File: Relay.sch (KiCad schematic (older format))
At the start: 11 parts

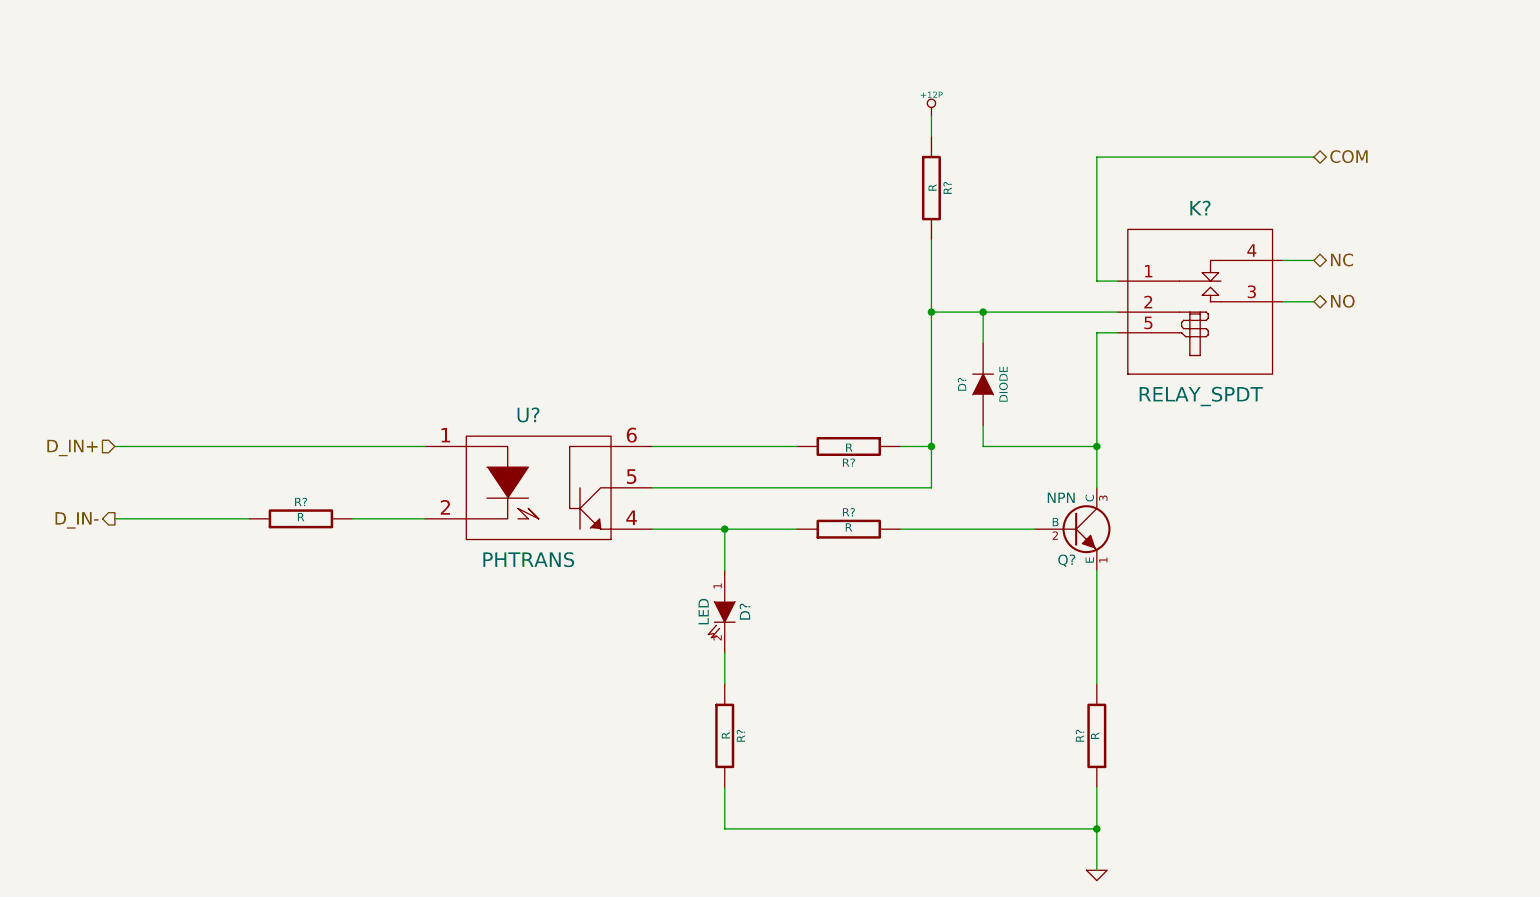
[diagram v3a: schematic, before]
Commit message: Completed Arduino Block Diagram and Fan Redesign
The commits as of this are now up to date with the videos released for
Contextual Electronics, Week 3.
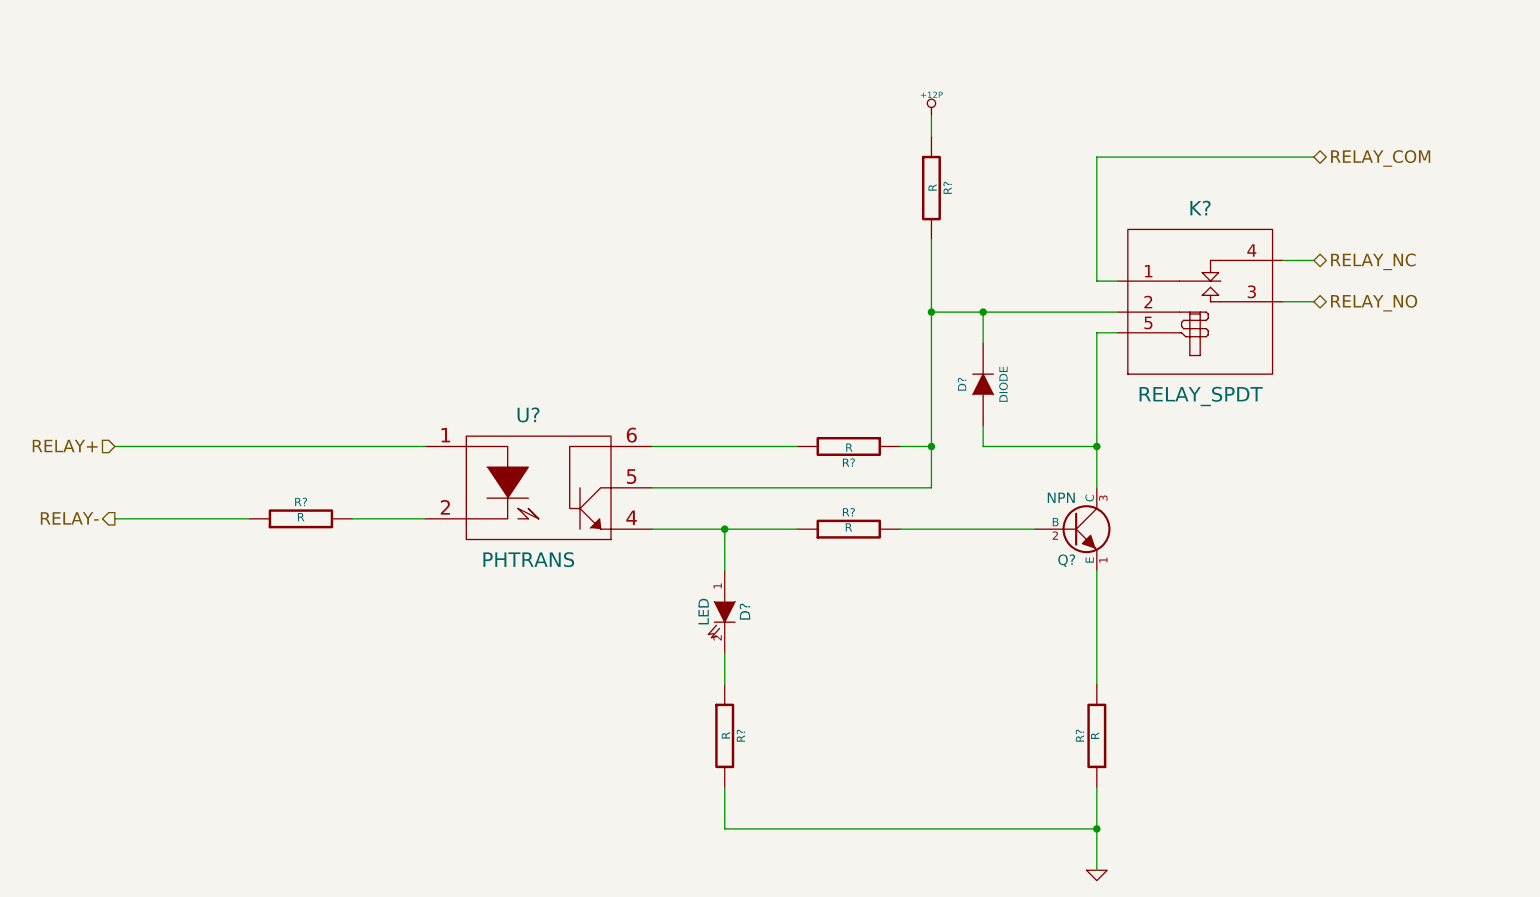
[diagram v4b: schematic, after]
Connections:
- net COM renamed RELAY_COM
- net D_IN+ renamed RELAY+
- net D_IN- renamed RELAY-
- net NC renamed RELAY_NC
- net NO renamed RELAY_NO
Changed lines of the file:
@@
 $Descr A4 11693 8268
 encoding utf-8
-Sheet 4 9
+Sheet 3 9
 Title ""
 Date "6 feb 2014"
@@
 $EndDescr
 Text HLabel 2350 3700 0    60   Input ~ 0
-D_IN+
+RELAY+
 Text HLabel 2350 4050 0    60   Output ~ 0
-D_IN-
+RELAY-
 Text HLabel 8150 2800 2    60   BiDi ~ 0
-NC
+RELAY_NC
 Text HLabel 8150 3000 2    60   BiDi ~ 0
-NO
+RELAY_NO
 $Comp
 L PHTRANS U?
@@
 $EndComp
 Text HLabel 8150 2300 2    60   BiDi ~ 0
-COM
+RELAY_COM
 Wire Wire Line
 	8150 2800 8000 2800

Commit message: Initial layout of relay and thermocouple
All block diagrams completed through Week 3.  Component selection
spreadsheets created: Bench Buddy Session 1CE.xlsx = official part
selection and bom.xlsx is the version I came up with.

Part association and initial layout of the Relay and Thermocouple
sections completed.
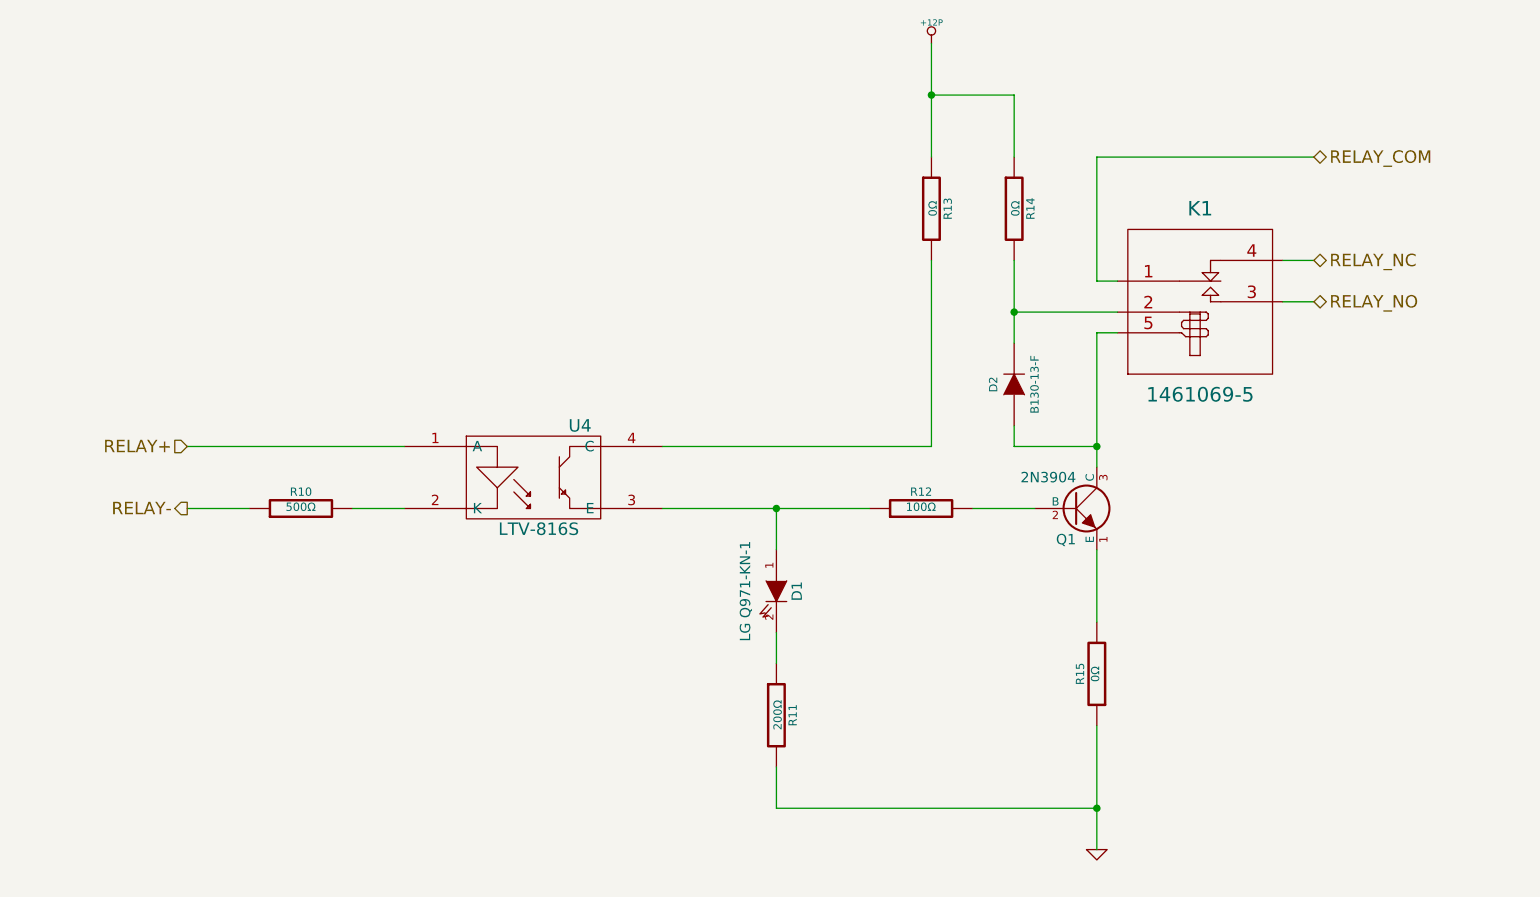
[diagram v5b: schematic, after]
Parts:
- removed R?: R, ~, symbol R
- removed U?: PHTRANS, ~, symbol PHTRANS
- added R14: 0Ω, ~, symbol R
- added U4: LTV-816S, symbol OPTO-TRANSISTOR4
- D1: renamed from D?; value LED -> LG Q971-KN-1; Distrib Part Num 1 (none) -> 475-1409-1; Distrib Part Num 1 Link (none) -> http://www.digikey.com/product-detail/en/LG%20Q971-KN-1/475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; MFG Name (none) -> OSRAM Opto Semi; MFG Part Num (none) -> LG Q971-KN-1
- D2: renamed from D?; value DIODE -> B130-13-F; Distrib Part Num 1 (none) -> B130-FDICT; Distrib Part Num 1 Link (none) -> http://www.digikey.com/product-detail/en/B130-13-F/B130-FDI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; MFG Name (none) -> Diodes Inc.; MFG Part Num (none) -> B130-13-F
- K1: renamed from K?; value RELAY_SPDT -> 1461069-5; Distrib Part Num 1 (none) -> PB1321; Distrib Part Num 1 Link (none) -> http://www.digikey.com/product-detail/en/1461069-5/PB1321-N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; MFG Name (none) -> TE Connectivity; MFG Part Num (none) -> 1461069-5
- Q1: renamed from Q?; value NPN -> 2N3904; Distrib Part Num 1 (none) -> MMBT3904-FDICT; Distrib Part Num 1 Link (none) -> http://www.digikey.com/product-detail/en/MMBT3904-7-F/MMBT3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; MFG Name (none) -> Diodes Inc.; MFG Part Num (none) -> MMBT3904-7-F
- R10: renamed from R?; value R -> 500Ω
- R11: renamed from R?; value R -> 200Ω
- R12: renamed from R?; value R -> 100Ω
- R13, R15: renamed from R?; value R -> 0Ω
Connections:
- net +12P: now also R14.1
- net RELAY+: now also U4.1 (A)
- net at R10.2: now also U4.2 (K)
- net at D1.1 (A), R12.1: now also U4.3 (E)
- net at D2.2 (K), K1.2 (COIL+): now also R14.2; no longer R13.2
- new net: R13.2, U4.4 (C)
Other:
- moved on the sheet: D1, D2, Q1, R10, R11, R12, R13, R15
